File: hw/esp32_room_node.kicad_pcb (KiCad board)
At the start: 2 copper layers, 6 x 8 mm, 7 parts, among them U1 DHT11, U2 HTU21

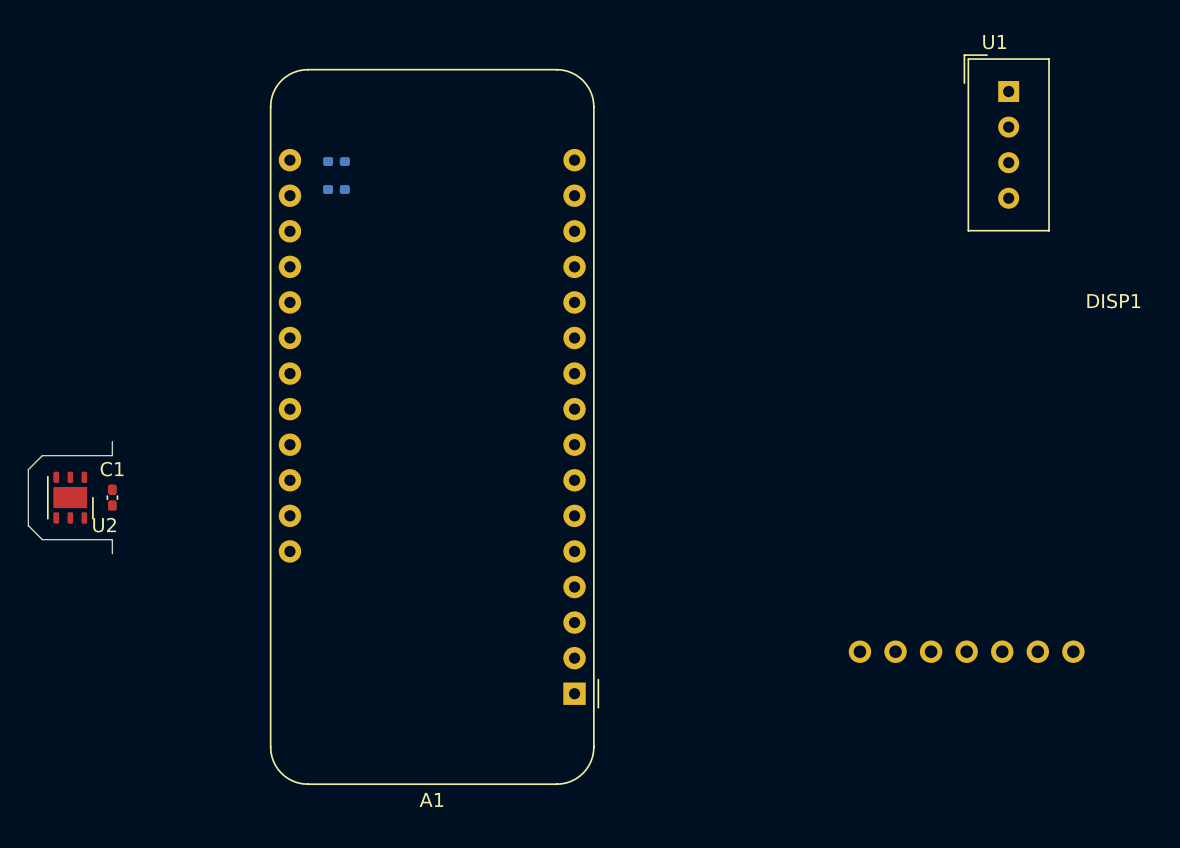
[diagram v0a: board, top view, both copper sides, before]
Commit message: Add encoder to schematic, outline
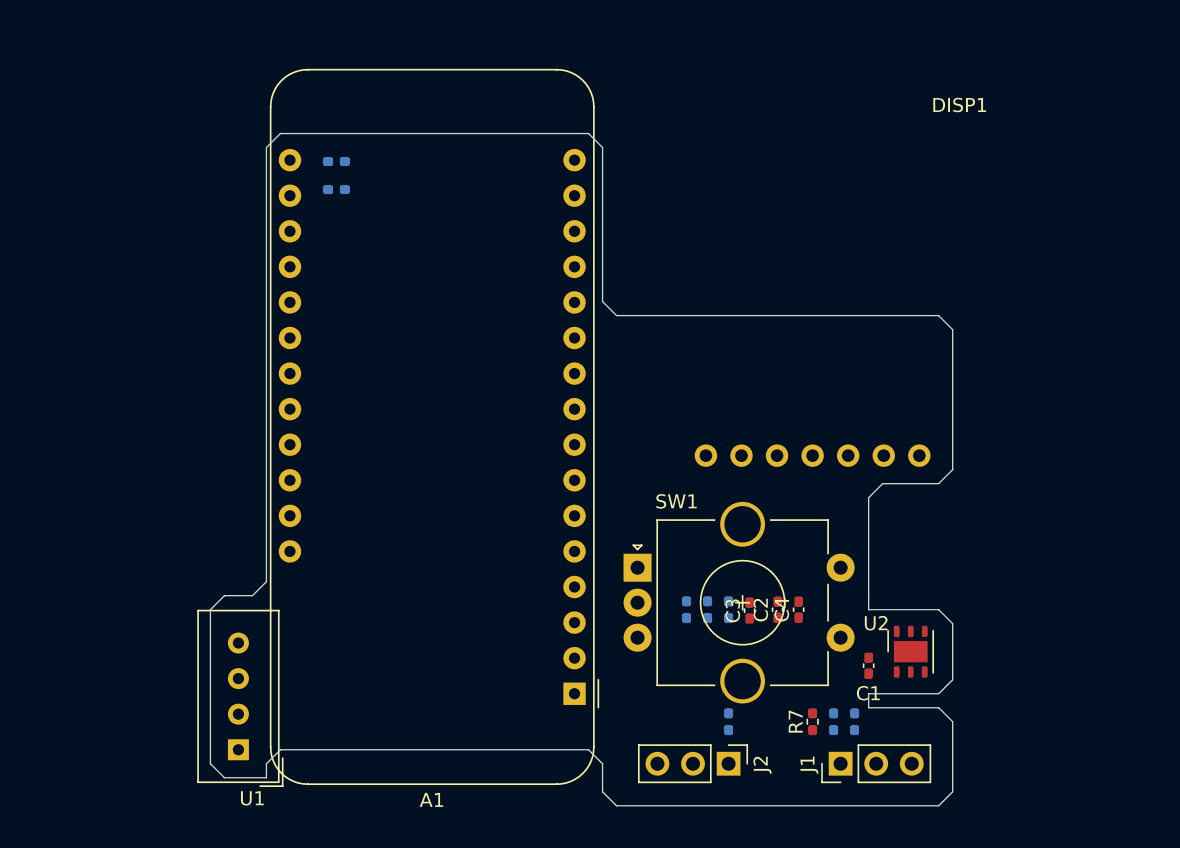
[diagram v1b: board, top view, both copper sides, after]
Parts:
- added C2: DNP, Capacitor_SMD:C_0402_1005Metric_Pad0.74x0.62mm_HandSolder, F.Cu at (179.5, 112.0)
- added C3: DNP, Capacitor_SMD:C_0402_1005Metric_Pad0.74x0.62mm_HandSolder, F.Cu at (177.5, 112.1)
- added C4: DNP, Capacitor_SMD:C_0402_1005Metric_Pad0.74x0.62mm_HandSolder, F.Cu at (181.0, 112.0)
- added J1: Conn_01x03, Connector_PinHeader_2.54mm:PinHeader_1x03_P2.54mm_Vertical, F.Cu at (184.0, 123.0)
- added J2: Conn_01x03, Connector_PinHeader_2.54mm:PinHeader_1x03_P2.54mm_Vertical, F.Cu at (176.0, 123.0)
- added R3: 4k7, Resistor_SMD:R_0402_1005Metric_Pad0.72x0.64mm_HandSolder, B.Cu at (183.5, 120.0)
- added R4: R, Resistor_SMD:R_0402_1005Metric_Pad0.72x0.64mm_HandSolder, B.Cu at (174.5, 112.0)
- added R5: R, Resistor_SMD:R_0402_1005Metric_Pad0.72x0.64mm_HandSolder, B.Cu at (173.0, 112.0)
- added R6: R, Resistor_SMD:R_0402_1005Metric_Pad0.72x0.64mm_HandSolder, B.Cu at (176.0, 112.0)
- added R7: 10, Resistor_SMD:R_0402_1005Metric_Pad0.72x0.64mm_HandSolder, F.Cu at (182.0, 120.0)
- added R8: 10, Resistor_SMD:R_0402_1005Metric_Pad0.72x0.64mm_HandSolder, B.Cu at (185.0, 120.0)
- added R9: 10, Resistor_SMD:R_0402_1005Metric_Pad0.72x0.64mm_HandSolder, B.Cu at (176.0, 120.0)
- added SW1: Rotary_Encoder_Switch, Rotary_Encoder:RotaryEncoder_Alps_EC11E-Switch_Vertical_H20mm_CircularMountingHoles, F.Cu at (169.5, 109.0)
- moved U1 72.3 mm to (141.0, 122.0), turned to 180 degrees
- moved U2 61.0 mm to (189.0, 115.0), turned to 90 degrees
- moved C1 55.3 mm to (186.0, 116.0), turned to 270 degrees
- moved DISP1 17.8 mm to (182.0, 101.0)
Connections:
- A1 pad 20: (no net) -> /LCD_BL
- A1 pad 22: (no net) -> /ONEWIRE
- A1 pad 23: (no net) -> /SERVO
- A1 pad 7: (no net) -> /ENC_BTN
- A1 pad 8: (no net) -> /ENC_A
- A1 pad 9: (no net) -> /ENC_B
- DISP1 pad 6: (no net) -> /LCD_BL
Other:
- board size 6 x 8 mm -> 53 x 48 mm

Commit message: Routed PCB
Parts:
- added H1: MountingHole, MountingHole:MountingHole_2.5mm, F.Cu at (189.5, 93.5)
- added H2: MountingHole, MountingHole:MountingHole_2.5mm, F.Cu at (189.5, 105.5)
- added LOGO1: Logo_Open_Hardware_Small, Symbol:OSHW-Logo_5.7x6mm_SilkScreen, B.Cu at (147.5, 114.0)
- added LOGO2: Logo_Open_Hardware_Small, elemental:elemental-4mm-mask, F.Cu at (169.5, 99.5)
- added LOGO3: Logo_Open_Hardware_Small, elemental:elemental-25.4mm, B.Cu at (152.0, 96.6)
- added TP1: TestPoint, TestPoint:TestPoint_THTPad_1.5x1.5mm_Drill0.7mm, B.Cu at (141.0, 102.9)
- added TP10: TestPoint, TestPoint:TestPoint_THTPad_1.5x1.5mm_Drill0.7mm, B.Cu at (161.3, 102.9)
- added TP11: TestPoint, TestPoint:TestPoint_THTPad_1.5x1.5mm_Drill0.7mm, B.Cu at (161.3, 100.3)
- added TP12: TestPoint, TestPoint:TestPoint_THTPad_1.5x1.5mm_Drill0.7mm, B.Cu at (161.3, 87.6)
- added TP2: TestPoint, TestPoint:TestPoint_THTPad_1.5x1.5mm_Drill0.7mm, B.Cu at (141.0, 105.4)
- added TP3: TestPoint, TestPoint:TestPoint_THTPad_1.5x1.5mm_Drill0.7mm, B.Cu at (141.0, 108.0)
- added TP4: TestPoint, TestPoint:TestPoint_THTPad_1.5x1.5mm_Drill0.7mm, B.Cu at (141.0, 100.3)
- added TP5: TestPoint, TestPoint:TestPoint_THTPad_1.5x1.5mm_Drill0.7mm, B.Cu at (161.3, 80.0)
- added TP6: TestPoint, TestPoint:TestPoint_THTPad_1.5x1.5mm_Drill0.7mm, B.Cu at (161.3, 85.1)
- added TP7: TestPoint, TestPoint:TestPoint_THTPad_1.5x1.5mm_Drill0.7mm, B.Cu at (161.3, 82.5)
- added TP8: TestPoint, TestPoint:TestPoint_THTPad_1.5x1.5mm_Drill0.7mm, B.Cu at (161.3, 108.0)
- added TP9: TestPoint, TestPoint:TestPoint_THTPad_1.5x1.5mm_Drill0.7mm, B.Cu at (161.3, 105.4)
- A1: footprint Module:Adafruit_Feather -> Module:Adafruit_Feather_WithMountingHoles
- C2, C3, C4, R7: moved to B.Cu
- moved R1 36.5 mm to (154.0, 116.0), turned to 270 degrees
- moved R2 34.8 mm to (155.5, 116.0), turned to 270 degrees
- moved C2 5.59 mm to (174.0, 113.0), turned to 270 degrees
- moved C3 5.09 mm to (172.5, 113.0), turned to 270 degrees
- moved R6 4.92 mm to (180.5, 110.0)
- moved R4 2.06 mm to (174.0, 110.0)
- moved R5 2.06 mm to (172.5, 110.0)
- moved U2 2.00 mm to (189.0, 117.0)
- moved C4 1.12 mm to (180.5, 113.0), turned to 270 degrees
- moved C1 0.50 mm to (186.0, 116.5)
- moved R9 0.50 mm to (175.5, 120.0), turned to 180 degrees
- turned R8 to 270 degrees
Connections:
- A1 pad 10: (no net) -> Net-(A1-Pad10)
- A1 pad 14: (no net) -> Net-(A1-Pad14)
- A1 pad 15: (no net) -> Net-(A1-Pad15)
- A1 pad 16: (no net) -> Net-(A1-Pad16)
- A1 pad 25: (no net) -> Net-(A1-Pad25)
- A1 pad 5: (no net) -> Net-(A1-Pad5)
- A1 pad 6: (no net) -> Net-(A1-Pad6)
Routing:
- net GND: track 0.00 -> 146.8 mm, vias 0 -> 4
- net +3V3: track 0.00 -> 96.0 mm, vias 0 -> 6
- net /SDA: track 0.00 -> 85.1 mm, vias 0 -> 1
- net /SCL: track 0.00 -> 81.6 mm, vias 0 -> 1
- net +5V: track 0.00 -> 67.2 mm
- net /ONEWIRE: track 0.00 -> 66.3 mm, vias 0 -> 4
- net /SERVO: track 0.00 -> 54.4 mm, vias 0 -> 2
- net /LCD_BL: track 0.00 -> 49.8 mm
- net /LCD_DC: track 0.00 -> 46.5 mm
- net /LCD_CS: track 0.00 -> 38.7 mm
- net /ENC_BTN: track 0.00 -> 32.1 mm, vias 0 -> 1
- net /SENS_DATA: track 0.00 -> 28.0 mm
- net /ENC_B: track 0.00 -> 27.3 mm
- net /ENC_A: track 0.00 -> 22.6 mm, vias 0 -> 1
- net /LCD_MOSI: track 0.00 -> 21.5 mm
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- added copper zone on B.Cu, net GND
- added copper zone on F.Cu, net GND
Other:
- board size 53 x 48 mm -> 53 x 53 mm
- net class Default: trace_width 0.25 -> 0.2
- net class Power added: clearance 0.2, trace_width 0.3, via_dia 0.8, via_drill 0.4
- board text added: "1"
- board text added: "1WIRE"
- board text added: "3V"
- board text added: "B"
- board text added: "DHT22"
- board text added: "ESP32 room node 2021 rev.A"
- board text added: "G"
- board text added: "HTU21"
- board text added: "R"
- board text added: "SERVO"
- board text added: "Y"

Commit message: Add prototype area
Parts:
- removed H2: MountingHole, MountingHole:MountingHole_2.5mm
- added PROTOAREA1: Logo_Open_Hardware_Small, Prototype area:protoarea, F.Cu at (176.0, 86.0)
- moved H1 12.0 mm to (189.5, 105.5)
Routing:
- net GND: track 146.8 -> 143.5 mm
- net /LCD_CS: track 38.7 -> 36.8 mm
- net /LCD_MOSI: track 21.5 -> 23.0 mm
- net /SCL: track 81.6 -> 80.3 mm
- net /SDA: track 85.1 -> 84.1 mm
- net +5V: track 67.2 -> 66.2 mm
- net /LCD_SCK: track 17.9 -> 18.5 mm
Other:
- board size 53 x 53 mm -> 53 x 52 mm
